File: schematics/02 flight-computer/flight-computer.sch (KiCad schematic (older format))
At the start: 41 parts, among them IC1 NCP4620, IC2 STM32F405RxTx, IC3 SL18860DC, J1 RJHSE-538x, J10 THERMO4, J11 PYRO1, J12 PYRO2, J13 PYRO_SI, J14 12V, J15 GND, J2 RJHSE-538x, J3 3V3, J4 GND, J5 PRESSURE1, J6 PRESSURE2, J7 THERMO1, J8 THERMO2, J9 THERMO3, P1 GPS, P2 TLM, P3 SWD_TC, Y1 TCXO

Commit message: Add preliminary pcb edges
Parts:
- removed C1, C11: 1u, cusf:0402, symbol cusf-kicad:C
- removed C12, C13: 100n, cusf:0402, symbol cusf-kicad:C
- removed D1, D2, D3, D4: ESD_DIODE, cusf:0402, symbol cusf-kicad:ESD_DIODE
- removed IC1: NCP4620, cusf:SC-70-5, symbol cusf-kicad:NCP4620
- removed IC2: STM32F405RxTx, cusf:LQFP-64, symbol cusf-kicad:STM32F405RxTx
- removed IC3: SL18860DC, cusf:DFN-10-SL18860DC, symbol cusf-kicad:SL18860DC
- removed J1, J2: RJHSE-538x, cusf:RJHSE-538X, symbol cusf-kicad:RJHSE-538x
- removed J10: THERMO4, cusf:B02B-PASK, symbol cusf-kicad:CONN_01x02
- removed J11: PYRO1, cusf:B02B-PASK, symbol cusf-kicad:CONN_01x02
- removed J12: PYRO2, cusf:B02B-PASK, symbol cusf-kicad:CONN_01x02
- removed J13: PYRO_SI, cusf:ULTRA-FIT-01x03, symbol cusf-kicad:CONN_01x03
- removed J14: 12V, cusf:ULTRA-FIT-01x03, symbol cusf-kicad:CONN_01x03
- removed J15, J4: GND, cusf:ULTRA-FIT-01x03, symbol cusf-kicad:CONN_01x03
- removed J3: 3V3, cusf:ULTRA-FIT-01x03, symbol cusf-kicad:CONN_01x03
- removed J5: PRESSURE1, cusf:B02B-PASK, symbol cusf-kicad:CONN_01x02
- removed J6: PRESSURE2, cusf:B02B-PASK, symbol cusf-kicad:CONN_01x02
- removed J7: THERMO1, cusf:B02B-PASK, symbol cusf-kicad:CONN_01x02
- removed J8: THERMO2, cusf:B02B-PASK, symbol cusf-kicad:CONN_01x02
- removed J9: THERMO3, cusf:B02B-PASK, symbol cusf-kicad:CONN_01x02
- removed P1: GPS, cusf:uFL-R-SMT, symbol cusf-kicad:COAX
- removed P2: TLM, cusf:uFL-R-SMT, symbol cusf-kicad:COAX
- removed R2: 10k, cusf:0402, symbol cusf-kicad:R
- removed Y1: TCXO, cusf:XTAL-25x20, symbol cusf-kicad:TCXO
- added C10: 100n, Strix:C_0402, symbol Strix:C
- added C11, C12: 10p, Strix:C_0402, symbol Strix:C
- added H1, H2, H3, H4: MountingHole_Pad, Strix:MountingHole_Pad, symbol Strix:MountingHole_Pad
- added IC1, IC2: MAX14787E, Strix:MAX14787E, symbol Strix:MAX14787E
- added J1, J2: UPPER CONN, symbol Strix:Conn_02x20
- added J3: BLACKBOX, symbol Strix:DB9
- added J4: SERIAL, symbol Strix:DB9
- added R2, R3: 120, Strix:R_0402, symbol Strix:R
- added U1: STM32F405RGT6, Strix:STM32F405RGT6, symbol Strix:STM32F405RGT6
- added Y1: XTAL, symbol Strix:XTAL
- C1: renamed from C8; footprint cusf:0402 -> Strix:C_0402; symbol cusf-kicad:C -> Strix:C
- C2: footprint cusf:0402 -> Strix:C_0402; symbol cusf-kicad:C -> Strix:C
- C3: renamed from C4; footprint cusf:0402 -> Strix:C_0402; symbol cusf-kicad:C -> Strix:C
- C4: renamed from C5; footprint cusf:0402 -> Strix:C_0402; symbol cusf-kicad:C -> Strix:C
- C5: renamed from C6; footprint cusf:0402 -> Strix:C_0402; symbol cusf-kicad:C -> Strix:C
- C6: renamed from C7; footprint cusf:0402 -> Strix:C_0402; symbol cusf-kicad:C -> Strix:C
- C7: renamed from C3; footprint cusf:0402 -> Strix:C_0402; symbol cusf-kicad:C -> Strix:C
- C8: renamed from C9; footprint cusf:0402 -> Strix:C_0402; symbol cusf-kicad:C -> Strix:C
- C9: renamed from C10; footprint cusf:0402 -> Strix:C_0402; symbol cusf-kicad:C -> Strix:C
- P1: renamed from P3; footprint cusf:TC2030-NL -> Strix:SWD_TC; symbol cusf-kicad:SWD_TC -> Strix:SWD_TC
- R1: value 10k -> 100; footprint cusf:0402 -> (none)
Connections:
- net 12v: now also J1.22 (Pin_22), J2.22 (Pin_22)
- net 1v8: now also J1.20 (Pin_20), J2.20 (Pin_20)
- net 3v3: now also IC1.1 (VDD), IC2.1 (VDD), J1.19 (Pin_19), J1.21 (Pin_21), J2.19 (Pin_19), J2.21 (Pin_21), J3.1, J3.5, J4.1, J4.5, U1.1 (VBAT), U1.13 (VDDA), U1.19 (VDD), U1.32 (VDD), U1.48 (VDD), U1.64 (VDD)
- net GND: now also C10.1, C11.1, C12.1, H1.1, H2.1, H3.1, H4.1, IC1.4 (GND), IC2.4 (GND), J1.1 (Pin_1), J1.2 (Pin_2), J1.3 (Pin_3), J1.37 (Pin_37), J1.38 (Pin_38), J1.39 (Pin_39), J1.4 (Pin_4), J1.40 (Pin_40), J2.1 (Pin_1), J2.2 (Pin_2), J2.3 (Pin_3), J2.37 (Pin_37), J2.38 (Pin_38), J2.39 (Pin_39), J2.4 (Pin_4), J2.40 (Pin_40), J3.0 (PAD), J3.3, J3.7, J3.8, J4.0 (PAD), J4.3, J4.7, J4.8, U1.12 (VSSA), U1.18 (VSS), U1.60 (BOOT0), U1.63 (VSS), Y1.2, Y1.4
- net I2C1_SCL: now also J1.23 (Pin_23), J2.23 (Pin_23), U1.58 (PB6)
- net I2C1_SDA: now also J1.24 (Pin_24), J2.24 (Pin_24), U1.59 (PB7)
- net SPI1_MISO: now also J1.11 (Pin_11), J2.11 (Pin_11), U1.22 (PA6)
- net SPI1_MOSI: now also J1.12 (Pin_12), J2.12 (Pin_12), U1.23 (PA7)
- net SPI1_SCLK: now also J1.10 (Pin_10), J2.10 (Pin_10), U1.21 (PA5)
- net SPI2_MISO: now also J1.17 (Pin_17), J2.17 (Pin_17), U1.35 (PB14)
- net SPI2_MOSI: now also J1.18 (Pin_18), J2.18 (Pin_18), U1.36 (PB15)
- net SPI2_SCLK: now also J1.15 (Pin_15), J2.15 (Pin_15), U1.34 (PB13)
- net SPI3_MISO: now also J1.32 (Pin_32), J2.32 (Pin_32), U1.52 (PC11)
- net SPI3_MOSI: now also J1.31 (Pin_31), J2.31 (Pin_31), U1.53 (PC12)
- net SPI3_SCLK: now also J1.34 (Pin_34), J2.34 (Pin_34), U1.51 (PC10)
- net SWDCLK: now also U1.49 (PA14)
- net SWDIO: now also U1.46 (PA13)
- net UART4_RX: now also IC2.2 (RO), U1.15 (PA1)
- net UART4_TX: now also IC2.3 (DI), U1.14 (PA0)
- net USART3_RX: now also J1.6 (Pin_6), J2.6 (Pin_6), U1.30 (PB11)
- net USART3_TX: now also J1.5 (Pin_5), J2.5 (Pin_5), U1.29 (PB10)
- net ~RST: now also C10.2, U1.7 (NRST)
- net at C8.2: now also U1.31 (VCAP_1)
- net at C9.2: now also U1.47 (VCAP_2)
- net at R1.1: now also C12.2, Y1.3
- net RADIO_CLK: no longer names the net of R1.2
- net RADIO_CLK: now also U1.6 (PH1)
- new net: C11.2, U1.5 (PH0), Y1.1
- new net GPIO_1: J1.7 (Pin_7), J2.7 (Pin_7), U1.26 (PB0)
- new net GPIO_10: J1.36 (Pin_36), J2.36 (Pin_36), U1.39 (PC8)
- new net GPIO_2: J1.8 (Pin_8), J2.8 (Pin_8), U1.27 (PB1)
- new net GPIO_3: J1.9 (Pin_9), J2.9 (Pin_9), U1.28 (PB2)
- new net GPIO_4: J1.25 (Pin_25), J2.25 (Pin_25), U1.16 (PA2)
- new net GPIO_5: J1.27 (Pin_27), J2.27 (Pin_27), U1.17 (PA3)
- new net GPIO_6: J1.29 (Pin_29), J2.29 (Pin_29), U1.20 (PA4)
- new net GPIO_7: J1.26 (Pin_26), J2.26 (Pin_26), U1.25 (PC5)
- new net GPIO_8: J1.28 (Pin_28), J2.28 (Pin_28), U1.37 (PC6)
- new net GPIO_9: J1.30 (Pin_30), J2.30 (Pin_30), U1.38 (PC7)
- new net INT_1: J1.13 (Pin_13), J2.13 (Pin_13), U1.8 (PC0)
- new net INT_2: J1.14 (Pin_14), J2.14 (Pin_14), U1.9 (PC1)
- new net INT_3: J1.16 (Pin_16), J2.16 (Pin_16), U1.10 (PC2)
- new net INT_4: J1.33 (Pin_33), J2.33 (Pin_33), U1.11 (PC3)
- new net INT_5: J1.35 (Pin_35), J2.35 (Pin_35), U1.24 (PC4)
- new net UART4_RX+: IC2.8 (A), J4.2, R3.1
- new net UART4_RX-: IC2.7 (B), J4.4, R3.2
- new net UART4_TX+: IC2.5 (Y), J4.6
- new net UART4_TX-: IC2.6 (Z), J4.9
- new net USART1_RX: IC1.2 (RO), U1.43 (PA10)
- new net USART1_RX+: IC1.8 (A), J3.2, R2.1
- new net USART1_RX-: IC1.7 (B), J3.4, R2.2
- new net USART1_TX: IC1.3 (DI), U1.42 (PA9)
- new net USART1_TX+: IC1.5 (Y), J3.6
- new net USART1_TX-: IC1.6 (Z), J3.9
- no-connect marks 18 -> 11
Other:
- note added: "Mounting Holes"
- note added: "UART4 <-> RS-422"
- note added: "USART1 <-> RS-422"
- note added: "Upper Board Connector (Female)"
- note removed: "1v8 Power"
- note removed: "26MHz Oscillator"
- note removed: "Antennas (U.FL)"
- note removed: "Arming Switch In (Molex)"
- note removed: "Clock Buffer"
- note removed: "Clock Distribution"
- note removed: "FIXME: No LEDs\nConnected Here"
- note removed: "MCU SERIAL INTERFACES\nSPI1: IMUs USART3: Serial Out\nSPI2: Radio UART4: GPS\nSPI3: Sensors + External"
- note removed: "Metrons (Molex)"
- note removed: "Power Connectors (Molex)"
- note removed: "RS-485 Out (RJ45)"
- note removed: "SPI Out (RJ45)"
- note removed: "Sensors (Molex)"
- moved on the sheet: C1, C2, C3, C4, C5, C6, C7, C8, C9, P1

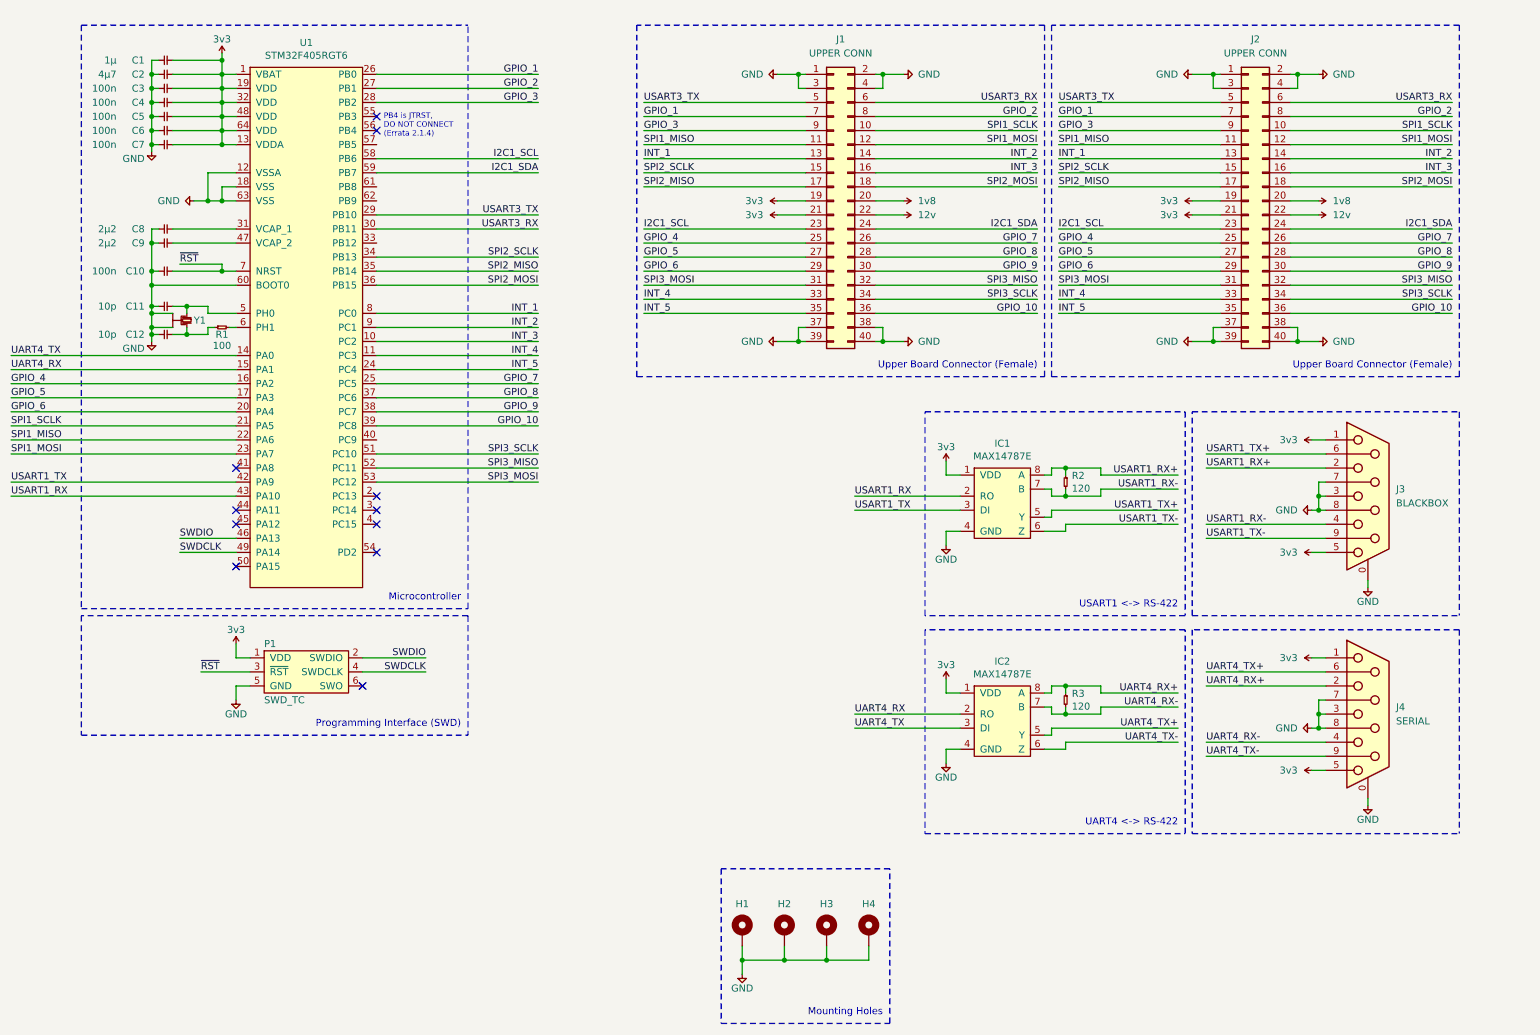
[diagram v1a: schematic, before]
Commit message: Add I2C pullups to flight computer
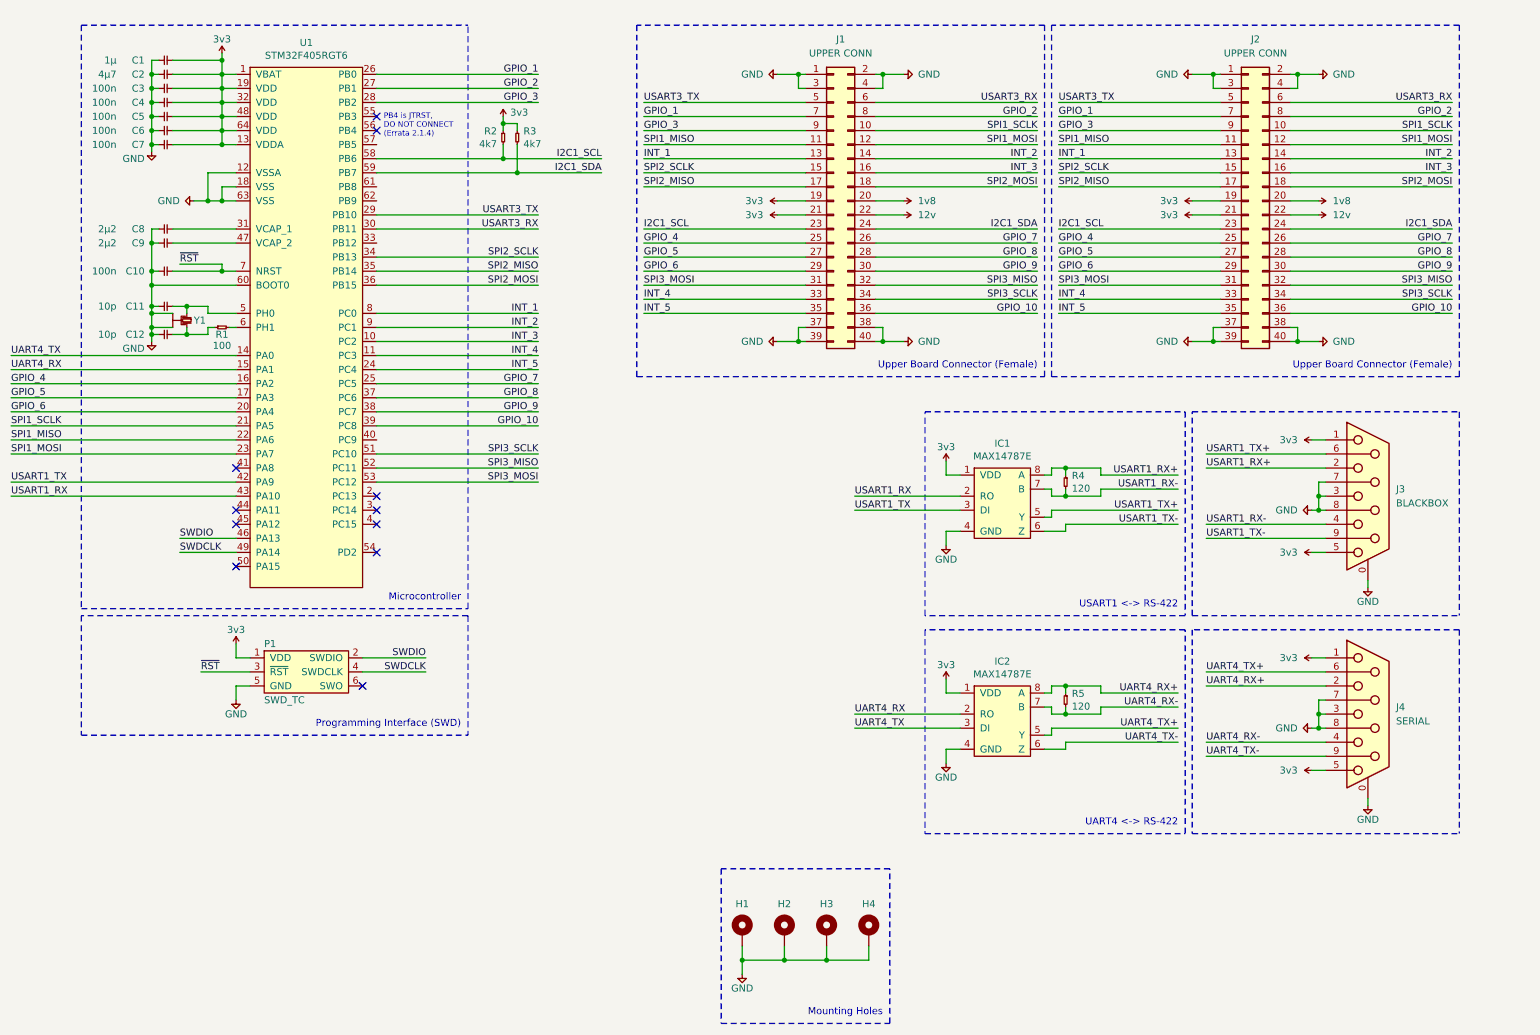
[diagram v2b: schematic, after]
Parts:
- added R2, R3: 4k7, Strix:R_0402, symbol Strix:R
- renumbered R2 to R4, R3 to R5
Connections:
- net 3v3: now also R2.1, R3.1
- net I2C1_SCL: now also R2.2
- net I2C1_SDA: now also R3.2
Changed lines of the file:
@@
 	8000 5500 8050 5500
 $Comp
-L Strix:R R3
+L Strix:R R5
 U 1 1 618D7B1A
 P 8150 5400
-AR Path="/618D7B1A" Ref="R3"  Part="1"
+AR Path="/618D7B1A" Ref="R5"  Part="1"
 AR Path="/62013BB2/618D7B1A" Ref="R?"  Part="1"
-F 0 "R3" V 8154 5444 50  0000 L CNN
+F 0 "R5" V 8154 5444 50  0000 L CNN
 F 1 "120" V 8245 5444 50  0000 L CNN
 F 2 "Strix:R_0402" H 8150 5400 50  0001 C CNN
@@
 	8000 3950 8050 3950
 $Comp
-L Strix:R R2
+L Strix:R R4
 U 1 1 615D4399
 P 8150 3850
-AR Path="/615D4399" Ref="R2"  Part="1"
+AR Path="/615D4399" Ref="R4"  Part="1"
 AR Path="/62013BB2/615D4399" Ref="R?"  Part="1"
-F 0 "R2" V 8154 3894 50  0000 L CNN
+F 0 "R4" V 8154 3894 50  0000 L CNN
 F 1 "120" V 8245 3894 50  0000 L CNN
 F 2 "Strix:R_0402" H 8150 3850 50  0001 C CNN
@@
 Connection ~ 9950 5650
 Wire Wire Line
-	4400 1700 3250 1700
-Wire Wire Line
-	3250 1600 4400 1600
-Text Label 4400 1600 2    50   ~ 0
+	4850 1700 4250 1700
+Wire Wire Line
+	3250 1600 4150 1600
+Text Label 4850 1600 2    50   ~ 0
 I2C1_SCL
-Text Label 4400 1700 2    50   ~ 0
+Text Label 4850 1700 2    50   ~ 0
 I2C1_SDA
 Wire Wire Line
@@
 Text Notes 10900 3100 2    50   ~ 0
 Upper Board Connector (Female)
+$Comp
+L Strix:R R2
+U 1 1 618CB7F3
+P 4150 1400
+AR Path="/618CB7F3" Ref="R2"  Part="1"
+AR Path="/62013BB2/618CB7F3" Ref="R?"  Part="1"
+F 0 "R2" V 4154 1444 50  0000 L CNN
+F 1 "4k7" V 4245 1444 50  0000 L CNN
+F 2 "Strix:R_0402" H 4150 1400 50  0001 C CNN
+F 3 "" H 4150 1400 50  0001 C CNN
+	1    4150 1400
+	0    -1   1    0
+$EndComp
+$Comp
+L Strix:R R3
+U 1 1 618CC569
+P 4250 1400
+AR Path="/618CC569" Ref="R3"  Part="1"
+AR Path="/62013BB2/618CC569" Ref="R?"  Part="1"
+F 0 "R3" V 4254 1444 50  0000 L CNN
+F 1 "4k7" V 4345 1444 50  0000 L CNN
+F 2 "Strix:R_0402" H 4250 1400 50  0001 C CNN
+F 3 "" H 4250 1400 50  0001 C CNN
+	1    4250 1400
+	0    1    1    0
+$EndComp
+Wire Wire Line
+	4250 1500 4250 1700
+Connection ~ 4250 1700
+Wire Wire Line
+	4250 1700 3250 1700
+Wire Wire Line
+	4150 1500 4150 1600
+Connection ~ 4150 1600
+Wire Wire Line
+	4150 1600 4850 1600
+Wire Wire Line
+	4150 1400 4150 1350
+Wire Wire Line
+	4150 1350 4250 1350
+Wire Wire Line
+	4250 1350 4250 1400
+$Comp
+L Strix:3v3 #PWR?
+U 1 1 6197418E
+P 4150 1300
+AR Path="/6013AE2F/6197418E" Ref="#PWR?"  Part="1"
+AR Path="/6197418E" Ref="#PWR?"  Part="1"
+AR Path="/605DF50F/6197418E" Ref="#PWR?"  Part="1"
+AR Path="/6013AEF4/6197418E" Ref="#PWR?"  Part="1"
+F 0 "#PWR?" H 4150 1410 50  0001 L CNN
+F 1 "3v3" H 4200 1300 50  0000 L BNN
+F 2 "" H 4150 1300 50  0001 C CNN
+F 3 "" H 4150 1300 50  0001 C CNN
+	1    4150 1300
+	1    0    0    -1
+$EndComp
+Wire Wire Line
+	4150 1300 4150 1350
+Connection ~ 4150 1350
 $EndSCHEMATC

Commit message: First attempt at layout
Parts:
- removed C10: 100n, Strix:C_0402, symbol Strix:C
- removed H2, H3, H4: MountingHole_Pad, Strix:MountingHole_Pad, symbol Strix:MountingHole_Pad
- removed J1, J2: UPPER CONN, symbol Strix:Conn_02x20
- removed J3: BLACKBOX, symbol Strix:DB9
- removed J4: SERIAL, symbol Strix:DB9
- added J1: CONN 1 UP, Strix:TFML-110-02-L-D, symbol Strix:Conn_02x10
- added J2: CONN 2 UP, Strix:TFML-110-02-L-D, symbol Strix:Conn_02x10
- added J3: CONN 1 DOWN, Strix:SFML-110-02-L-D-LC, symbol Strix:Conn_02x10
- added J4: CONN 2 DOWN, Strix:SFML-110-02-L-D-LC, symbol Strix:Conn_02x10
- added J5: SERIAL 1, Strix:Molex_PicoBlade_53261-0871, symbol Strix:Conn_01x08
- added J6: SERIAL 2, Strix:Molex_PicoBlade_53261-0871, symbol Strix:Conn_01x08
- H1: footprint Strix:MountingHole_Pad -> Strix:MountingHole_M2_Pad
- R1: footprint (none) -> Strix:R_0402
- Y1: footprint (none) -> Strix:XTAL-20x16
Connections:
- net 12v: now also J2.18 (Pin_18), J4.18 (Pin_18)
- net 1v8: now also J1.4 (Pin_4), J3.4 (Pin_4)
- net 3v3: now also J1.1 (Pin_1), J1.2 (Pin_2), J2.19 (Pin_19), J2.20 (Pin_20), J3.1 (Pin_1), J3.2 (Pin_2), J4.19 (Pin_19), J4.20 (Pin_20), J5.1 (Pin_1), J5.2 (Pin_2), J6.1 (Pin_1), J6.2 (Pin_2)
- net GND: now also J1.19 (Pin_19), J1.20 (Pin_20), J2.1 (Pin_1), J2.2 (Pin_2), J3.19 (Pin_19), J3.20 (Pin_20), J4.1 (Pin_1), J4.2 (Pin_2), J5.7 (Pin_7), J5.8 (Pin_8), J6.7 (Pin_7), J6.8 (Pin_8)
- net GPIO_1: now also J1.7 (Pin_7), J3.7 (Pin_7)
- net GPIO_10: now also J2.16 (Pin_16), J4.16 (Pin_16)
- net GPIO_2: now also J1.8 (Pin_8), J3.8 (Pin_8)
- net GPIO_3: now also J1.9 (Pin_9), J3.9 (Pin_9)
- net GPIO_4: now also J2.5 (Pin_5), J4.5 (Pin_5)
- net GPIO_5: now also J2.7 (Pin_7), J4.7 (Pin_7)
- net GPIO_6: now also J2.9 (Pin_9), J4.9 (Pin_9)
- net GPIO_7: now also J2.6 (Pin_6), J4.6 (Pin_6)
- net GPIO_8: now also J2.8 (Pin_8), J4.8 (Pin_8)
- net GPIO_9: now also J2.10 (Pin_10), J4.10 (Pin_10)
- net I2C1_SCL: now also J2.3 (Pin_3), J4.3 (Pin_3)
- net I2C1_SDA: now also J2.4 (Pin_4), J4.4 (Pin_4)
- net INT_1: now also J1.13 (Pin_13), J3.13 (Pin_13)
- net INT_2: now also J1.14 (Pin_14), J3.14 (Pin_14)
- net INT_3: now also J1.16 (Pin_16), J3.16 (Pin_16)
- net INT_4: now also J2.13 (Pin_13), J4.13 (Pin_13)
- net INT_5: now also J2.15 (Pin_15), J4.15 (Pin_15)
- net SPI1_MISO: now also J1.11 (Pin_11), J3.11 (Pin_11)
- net SPI1_MOSI: now also J1.12 (Pin_12), J3.12 (Pin_12)
- net SPI1_SCLK: now also J1.10 (Pin_10), J3.10 (Pin_10)
- net SPI2_MISO: now also J1.17 (Pin_17), J3.17 (Pin_17)
- net SPI2_MOSI: now also J1.18 (Pin_18), J3.18 (Pin_18)
- net SPI2_SCLK: now also J1.15 (Pin_15), J3.15 (Pin_15)
- net SPI3_MISO: now also J2.12 (Pin_12), J4.12 (Pin_12)
- net SPI3_MOSI: now also J2.11 (Pin_11), J4.11 (Pin_11)
- net SPI3_SCLK: now also J2.14 (Pin_14), J4.14 (Pin_14)
- net UART4_RX+: now also J6.5 (Pin_5)
- net UART4_RX-: now also J6.6 (Pin_6)
- net UART4_TX+: now also J6.3 (Pin_3)
- net UART4_TX-: now also J6.4 (Pin_4)
- net USART1_RX+: now also J5.5 (Pin_5)
- net USART1_RX-: now also J5.6 (Pin_6)
- net USART1_TX+: now also J5.3 (Pin_3)
- net USART1_TX-: now also J5.4 (Pin_4)
- net USART3_RX: now also J1.6 (Pin_6), J3.6 (Pin_6)
- net USART3_TX: now also J1.5 (Pin_5), J3.5 (Pin_5)
- new net RSVD_1: J1.3 (Pin_3), J3.3 (Pin_3)
- new net RSVD_2: J2.17 (Pin_17), J4.17 (Pin_17)
- no-connect marks 11 -> 16
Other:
- note added: "Mounting Hole"
- note added: "Off-Board Connectors"
- note added: "SERIAL 1 OUT"
- note added: "SERIAL 2 OUT"
- note removed: "Mounting Holes"
- note removed: "Upper Board Connector (Female)"
- moved on the sheet: H1, IC1, IC2, R4, R5
